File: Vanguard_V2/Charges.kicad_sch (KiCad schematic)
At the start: 1 part, among them J6 Screw_Terminal_01x04

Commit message: started layout for V2.1
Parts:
- added D4, D5: D_Schottky, Diode_SMD:D_0603_1608Metric, symbol Device:D_Schottky
- added Q1: SI7232DN-T1-GE3, SI7232DNT1GE3, symbol VanguardLib:SI7232DN-T1-GE3
- added R10, R12: 10, Resistor_SMD:R_0402_1005Metric, symbol Device:R
- added R13, R14: 10k, Resistor_SMD:R_0402_1005Metric, symbol Device:R
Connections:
- net C2_M: now reaches J6.1 (Pin_1)
- net C2_M: now also Q1.5 (D2_1)
- net VIN: now reaches J6.2 (Pin_2)
- net VIN: now also J6.4 (Pin_4), D4.1 (K), D5.1 (K)
- net C1_M: now reaches J6.3 (Pin_3)
- net C1_M: now also Q1.7 (D1_1)
- new net: Q1.4 (G2), R12.2
- new net: Q1.2 (G1), R10.2
- new net C1_GATE: R10.1, R13.1
- new net C2_GATE: R12.1, R14.1
- new net GND: D4.2 (A), D5.2 (A), Q1.1 (S1), Q1.3 (S2), R13.2, R14.2

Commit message: Begun board routing
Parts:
- removed R10, R12: 10, Resistor_SMD:R_0402_1005Metric, symbol Device:R
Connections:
- net C1_GATE: now also Q1.2 (G1)
- net C2_GATE: now also Q1.4 (G2)
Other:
- moved on the sheet: Q1, R13

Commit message: Everything is placed
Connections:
- net C1_M: now also J6.1 (Pin_1), Q1.10 (D1_4), Q1.11 (D1_5), Q1.8 (D1_2), Q1.9 (D1_3); no longer J6.3 (Pin_3)
- net C2_M: now also J6.3 (Pin_3), Q1.12 (D2_3), Q1.13 (D2_4), Q1.14 (D2_5), Q1.6 (D2_2); no longer J6.1 (Pin_1)
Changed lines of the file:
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@@
+	)
+	(junction
+		(at 121.92 53.34)
+		(diameter 0)
+		(color 0 0 0 0)
+	)
+	(junction
+		(at 121.92 50.8)
+		(diameter 0)
+		(color 0 0 0 0)
 	)
 	(junction
@@
 	)
 	(junction
+		(at 121.92 43.18)
+		(diameter 0)
+		(color 0 0 0 0)
+	)
+	(junction
 		(at 21.59 54.61)
 		(diameter 0)
@@
 	)
 	(junction
+		(at 93.98 53.34)
+		(diameter 0)
+		(color 0 0 0 0)
+	)
+	(junction
+		(at 93.98 58.42)
+		(diameter 0)
+		(color 0 0 0 0)
+	)
+	(junction
 		(at 33.02 66.04)
 		(diameter 0)
@@
 		(color 0 0 0 0)
 	)
+	(junction
+		(at 121.92 45.72)
+		(diameter 0)
+		(color 0 0 0 0)
+	)
 	(wire
 		(pts
@@
 	(wire
 		(pts
+			(xy 121.92 53.34) (xy 121.92 55.88)
+		)
+		(stroke
+			(width 0)
+			(type default)
+		)
+	)
+	(wire
+		(pts
 			(xy 43.18 66.04) (xy 43.18 62.23)
 		)
@@
 	(wire
 		(pts
+			(xy 121.92 50.8) (xy 121.92 53.34)
+		)
+		(stroke
+			(width 0)
+			(type default)
+		)
+	)
+	(wire
+		(pts
 			(xy 34.29 91.44) (xy 34.29 93.98)
 		)
@@
 	(wire
 		(pts
+			(xy 93.98 58.42) (xy 93.98 60.96)
+		)
+		(stroke
+			(width 0)
+			(type default)
+		)
+	)
+	(wire
+		(pts
 			(xy 29.21 35.56) (xy 31.75 35.56)
 		)
@@
 	(wire
 		(pts
+			(xy 121.92 50.8) (xy 124.46 50.8)
+		)
+		(stroke
+			(width 0)
+			(type default)
+		)
+	)
+	(wire
+		(pts
 			(xy 43.18 96.52) (xy 43.18 93.98)
 		)
@@
 	(wire
 		(pts
+			(xy 93.98 53.34) (xy 93.98 55.88)
+		)
+		(stroke
+			(width 0)
+			(type default)
+		)
+	)
+	(wire
+		(pts
 			(xy 43.18 92.71) (xy 43.18 93.98)
 		)
@@
 	(wire
 		(pts
+			(xy 121.92 43.18) (xy 124.46 43.18)
+		)
+		(stroke
+			(width 0)
+			(type default)
+		)
+	)
+	(wire
+		(pts
 			(xy 93.98 43.18) (xy 68.58 43.18)
 		)
@@
 	(wire
 		(pts
+			(xy 121.92 43.18) (xy 121.92 45.72)
+		)
+		(stroke
+			(width 0)
+			(type default)
+		)
+	)
+	(wire
+		(pts
 			(xy 43.18 85.09) (xy 43.18 80.01)
 		)
@@
 	(wire
 		(pts
+			(xy 121.92 45.72) (xy 121.92 48.26)
+		)
+		(stroke
+			(width 0)
+			(type default)
+		)
+	)
+	(wire
+		(pts
 			(xy 27.94 83.82) (xy 34.29 83.82)
 		)
@@
 		)
 	)
+	(global_label "C1_M"
+		(shape input)
+		(at 124.46 43.18 0)
+		(fields_autoplaced yes)
+		(effects
+			(font
+				(size 1.27 1.27)
+			)
+			(justify left)
+		)
+		(property "Intersheetrefs" "${INTERSHEET_REFS}"
+			(at 132.3437 43.18 0)
+			(effects
+				(font
+					(size 1.27 1.27)
+				)
+				(justify left)
+				(hide yes)
+			)
+		)
+	)
 	(global_label "C1_GATE"
 		(shape input)
@@
 		)
 	)
+	(global_label "C2_P"
+		(shape input)
+		(at 31.75 33.02 0)
+		(fields_autoplaced yes)
+		(effects
+			(font
+				(size 1.27 1.27)
+			)
+			(justify left)
+		)
+		(property "Intersheetrefs" "${INTERSHEET_REFS}"
+			(at 39.4523 33.02 0)
+			(effects
+				(font
+					(size 1.27 1.27)
+				)
+				(justify left)
+				(hide yes)
+			)
+		)
+	)
+	(global_label "C2_M"
+		(shape input)
+		(at 91.44 53.34 180)
+		(fields_autoplaced yes)
+		(effects
+			(font
+				(size 1.27 1.27)
+			)
+			(justify right)
+		)
+		(property "Intersheetrefs" "${INTERSHEET_REFS}"
+			(at 83.5563 53.34 0)
+			(effects
+				(font
+					(size 1.27 1.27)
+				)
+				(justify right)
+				(hide yes)
+			)
+		)
+	)
+	(global_label "C1_M"
+		(shape input)
+		(at 31.75 40.64 0)
+		(fields_autoplaced yes)
+		(effects
+			(font
+				(size 1.27 1.27)
+			)
+			(justify left)
+		)
+		(property "Intersheetrefs" "${INTERSHEET_REFS}"
+			(at 39.6337 40.64 0)
+			(effects
+				(font
+					(size 1.27 1.27)
+				)
+				(justify left)
+				(hide yes)
+			)
+		)
+	)
+	(global_label "C2_M"
+		(shape input)
+		(at 124.46 50.8 0)
+		(fields_autoplaced yes)
+		(effects
+			(font
+				(size 1.27 1.27)
+			)
+			(justify left)
+		)
+		(property "Intersheetrefs" "${INTERSHEET_REFS}"
+			(at 132.3437 50.8 0)
+			(effects
+				(font
+					(size 1.27 1.27)
+				)
+				(justify left)
+				(hide yes)
+			)
+		)
+	)
 	(global_label "C1_P"
 		(shape input)
-		(at 31.75 33.02 0)
+		(at 31.75 38.1 0)
 		(fields_autoplaced yes)
 		(effects
@@
 		)
 		(property "Intersheetrefs" "${INTERSHEET_REFS}"
-			(at 39.4523 33.02 0)
+			(at 39.4523 38.1 0)
 			(effects
 				(font
@@
 	(global_label "C2_M"
 		(shape input)
-		(at 91.44 53.34 180)
-		(fields_autoplaced yes)
-		(effects
-			(font
-				(size 1.27 1.27)
-			)
-			(justify right)
-		)
-		(property "Intersheetrefs" "${INTERSHEET_REFS}"
-			(at 83.5563 53.34 0)
-			(effects
-				(font
-					(size 1.27 1.27)
-				)
-				(justify right)
-				(hide yes)
-			)
-		)
-	)
-	(global_label "C2_M"
-		(shape input)
-		(at 31.75 40.64 0)
-		(fields_autoplaced yes)
-		(effects
-			(font
-				(size 1.27 1.27)
-			)
-			(justify left)
-		)
-		(property "Intersheetrefs" "${INTERSHEET_REFS}"
-			(at 39.6337 40.64 0)
-			(effects
-				(font
-					(size 1.27 1.27)
-				)
-				(justify left)
-				(hide yes)
-			)
-		)
-	)
-	(global_label "C2_P"
-		(shape input)
-		(at 31.75 38.1 0)
-		(fields_autoplaced yes)
-		(effects
-			(font
-				(size 1.27 1.27)
-			)
-			(justify left)
-		)
-		(property "Intersheetrefs" "${INTERSHEET_REFS}"
-			(at 39.4523 38.1 0)
-			(effects
-				(font
-					(size 1.27 1.27)
-				)
-				(justify left)
-				(hide yes)
-			)
-		)
-	)
-	(global_label "C1_M"
-		(shape input)
 		(at 31.75 35.56 0)

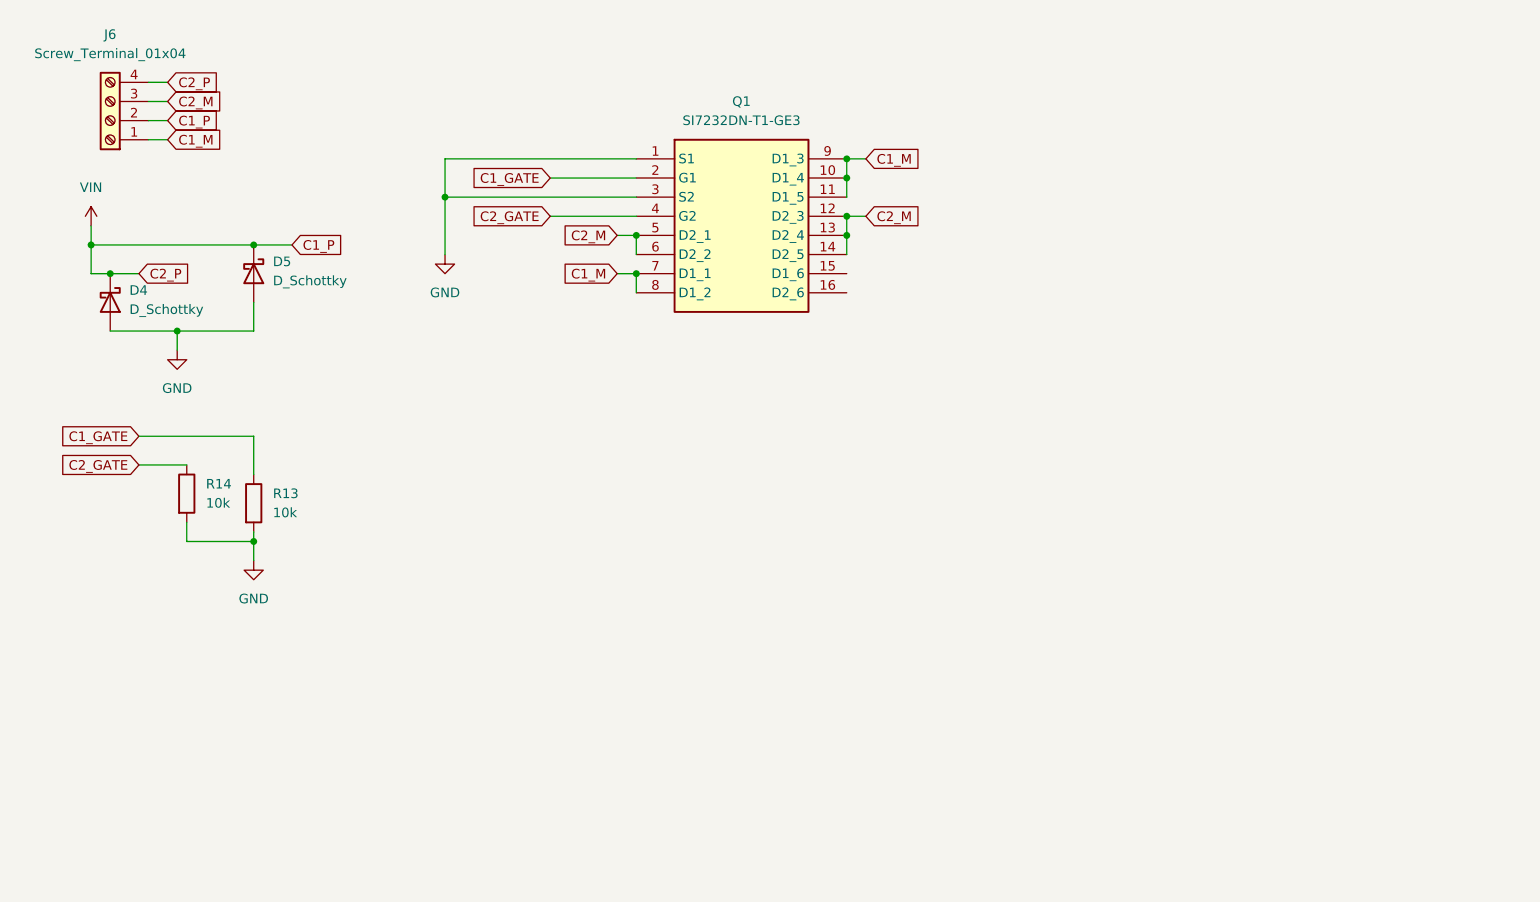
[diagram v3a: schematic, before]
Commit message: Added ejection charges
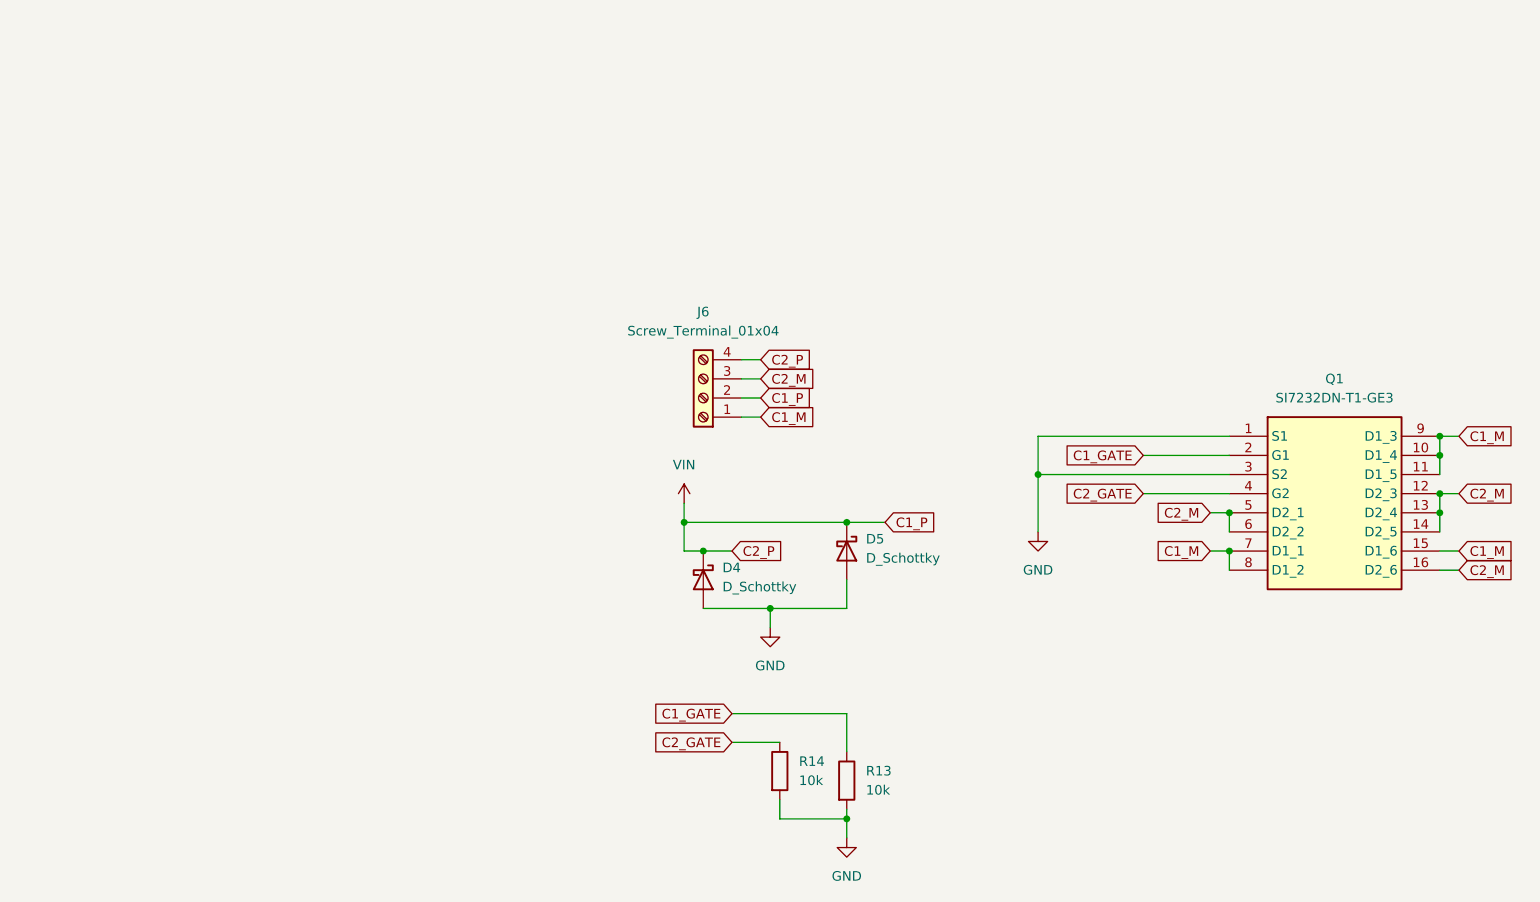
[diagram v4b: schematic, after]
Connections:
- net C1_M: now also Q1.15 (D1_6)
- net C2_M: now also Q1.16 (D2_6)
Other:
- moved on the sheet: D4, D5, J6, Q1, R13, R14
